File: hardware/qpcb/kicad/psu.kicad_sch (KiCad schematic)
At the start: 110 parts, among them IC1 ADM7150ARDZ-5.0-R7, IC2 ADM7150ARDZ-5.0-R7, IC3 ADM7150ARDZ-5.0-R7, IC4 ADM7150ARDZ-5.0-R7, IC5 TPS5450QDDARQ1, IC6 LT3083EQ#PBF, IC7 TPS5450QDDARQ1, IC8 LT3083EQ#PBF, J10 Conn_01x02, J3 Conn_01x02, J4 Conn_01x02, J5 Conn_01x02, J6 Conn_01x02, J7 Conn_01x02, J8 Conn_01x02, J9 Conn_01x02, Q1 2N7002, Q2 2N7002, Q3 2N7002, Q4 2N7002, Q5 2N7002, Q6 2N7002, U2 MC34063AD, U3 LM337T

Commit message: Complete PSU simulations and fix ERC errors
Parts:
- added C47, C48: C, symbol Device:C
- added C50: 0.1u, Capacitor_SMD:C_0805_2012Metric_Pad1.18x1.45mm_HandSolder, symbol Device:C_Polarized_US
- added C57, C58: 10u, Capacitor_SMD:C_0805_2012Metric_Pad1.18x1.45mm_HandSolder, symbol Device:C_Polarized_US
- added D10, D11, D12, D13, D14, D15, D16, D17: LED, symbol Device:LED
- added D18, D19, D20, D21, D24, D25: PMEG3050EP,115, symbol Device:D_Schottky
- added IC10: LT3083EQ#PBF, LT3083EQPBF, symbol LT3083EQ#PBF:LT3083EQ#PBF
- added J13, J14, J15, J16, J17: Conn_01x02, symbol Connector_Generic:Conn_01x02
- added L4, L5: L, symbol Device:L
- added R44, R45, R46, R47, R68, R69, R70, R71: R, symbol Device:R
- added R72, R73: TBD, symbol Device:R
- added TP1, TP10, TP11, TP12, TP2, TP3, TP4, TP5, TP6, TP7, TP8, TP9: TestPoint, symbol Connector:TestPoint
- R30: value 100k -> 120k
- R31: value 100k -> 6k
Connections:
- net -3V3: now also C37.2, R12.2, U3.3 (OUT), D17.1 (K)
- net 12V: now also R45.1
- net 12V_EN: now also TP1.1; no longer R31.2
- net 24V: now also J13.1 (Pin_1), R44.1
- net 3V3_A: now also R69.1
- net 3V3_A_EN: now also TP5.1
- net 3V3_B: now also R70.1
- net 3V3_B_EN: now also TP6.1
- net 3V3_RASP: no longer R30.1, R31.1
- net 5V_A: now also R47.1
- net 5V_A_EN: now also TP3.1
- net 5V_B: now also R68.1
- net 5V_B_EN: now also TP4.1
- net 6V: now also R46.1
- net 6V_EN: now also TP2.1; no longer R30.2
- net GND: now also R30.1, R31.1, C47.1, C48.1, C50.2, C57.2, C58.2, D10.1 (K), D11.1 (K), D12.1 (K), D13.1 (K), D14.1 (K), D15.1 (K), D16.1 (K), IC10.1 (NC), J13.2 (Pin_2), J14.2 (Pin_2), J15.2 (Pin_2), J16.2 (Pin_2), J17.2 (Pin_2), R71.1, R72.1, R73.1
- net 6V_AUX: now reaches C15.1, IC3.8 (VIN), R16.1
- net 6V_AUX: now also C20.1, IC4.8 (VIN), R17.1, R31.2, C58.1, IC10.3 (OUT_1), IC10.6 (OUT_2), J17.1 (Pin_1)
- net -6V_INT: now reaches C25.2, C26.2, D2.2 (A), R5.1, U2.4 (GND)
- net -6V_INT: now also D20.2 (A), TP11.1
- net 8V: now reaches C1.1, IC1.8 (VIN), R14.1
- net 8V: now also C10.1, C21.1, C24.1, IC2.8 (VIN), IC6.4 (VCONTROL), IC6.5 (IN), R15.1, R4.2, U2.6 (Vin), C57.1, D18.1 (K), D19.1 (K), IC10.4 (VCONTROL), IC10.5 (IN), TP8.1
- net -6V: now reaches C36.2, U3.2 (IN)
- net -6V: now also D20.1 (K), D21.1 (K), TP12.1
- net 13V5: no longer names the net of C30.1, L3.1, R8.2
- net 13V5: now also L5.1; no longer C34.1, IC8.4 (VCONTROL), IC8.5 (IN)
- net 7V5: no longer names the net of C29.1, L1.1, R3.2
- net 7V5: now also L4.1; no longer C21.1, IC6.4 (VCONTROL), IC6.5 (IN)
- new net: D13.2 (A), R47.2
- new net: C50.1, IC10.2 (SET), R30.2
- new net: D12.2 (A), R46.2
- new net: D14.2 (A), R68.2
- new net: D11.2 (A), R45.2
- new net: D10.2 (A), R44.2
- new net: D16.2 (A), R70.2
- new net: D15.2 (A), R69.2
- new net: D17.2 (A), R71.2
- new net -6V_EXT: D21.2 (A), J16.1 (Pin_1)
- new net 14V: C34.1, D24.1 (K), D25.1 (K), IC8.4 (VCONTROL), IC8.5 (IN), TP10.1
- new net 14V_EXT: D25.2 (A), J14.1 (Pin_1)
- new net 14V_INT: C48.2, D24.2 (A), L5.2, R73.2, TP9.1
- new net 8V_EXT: D19.2 (A), J15.1 (Pin_1)
- new net 8V_INT: C47.2, D18.2 (A), L4.2, R72.2, TP7.1
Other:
- note added: "Power input connectors"
- note added: "Power output connectors"
- note added: "Power-good LEDs"
- note added: "Test-points"
- note added: "The TPS5450-Q1 circuit was designed using TI WEBENCH POWER DESIGNER. The design can be obtained at the following link: https://webench.ti.com/appinfo/webench/scripts/SDP.cgi?ID=2D7513C0D29458C6"
- note added: "The TPS5450-Q1 circuit was designed using TI WEBENCH POWER DESIGNER. The design can be obtained at the following link: https://webench.ti.com/appinfo/webench/scripts/SDP.cgi?ID=5E5784C9527CE6F4"
- note added: "The input 24V is first converted to 14V using the TPS5450-Q1 switching voltage regulator. Then, it is further converted to 12V using the LT3083 linear voltage regulator. 14V input voltage is required to guarantee the minimum voltage dropout of the schottky diode and of the LT3083."
- note added: "The input 24V is first converted to 8V using the TPS5450-Q1 switching voltage regulator. Then, it is further converted to 6V using the LT3083 linear voltage regulator. 8V input voltage is required to guarantee the minimum voltage dropout of the schottky diode and of the LT3083."
- note removed: "The TPS5450-Q1 circuit was designed using TI WEBENCH POWER DESIGNER. The design can be obtained at the following link: https://webench.ti.com/appinfo/webench/scripts/SDP.cgi?ID=1DBFA0CBE6476B5C"
- note removed: "The TPS5450-Q1 circuit was designed using TI WEBENCH POWER DESIGNER. The design can be obtained at the following link: https://webench.ti.com/appinfo/webench/scripts/SDP.cgi?ID=32DE457FE0809D28"
- note removed: "The input 24V is first converted to 13.5V using the TPS5450-Q1 switching voltage regulator. Then, it is further converted to 12V using the LT3083 linear voltage regulator. 13.5V input voltage is required to guarantee the minimum voltage dropout."
- note removed: "The input 24V is first converted to 7.5V using the TPS5450-Q1 switching voltage regulator. Then, it is further converted to 6V using the LT3083 linear voltage regulator. 7.5V input voltage is required to guarantee the minimum voltage dropout."
- moved on the sheet: C1, C10, C11, C12, C13, C14, C15, C16, C17, C18, C19, C2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

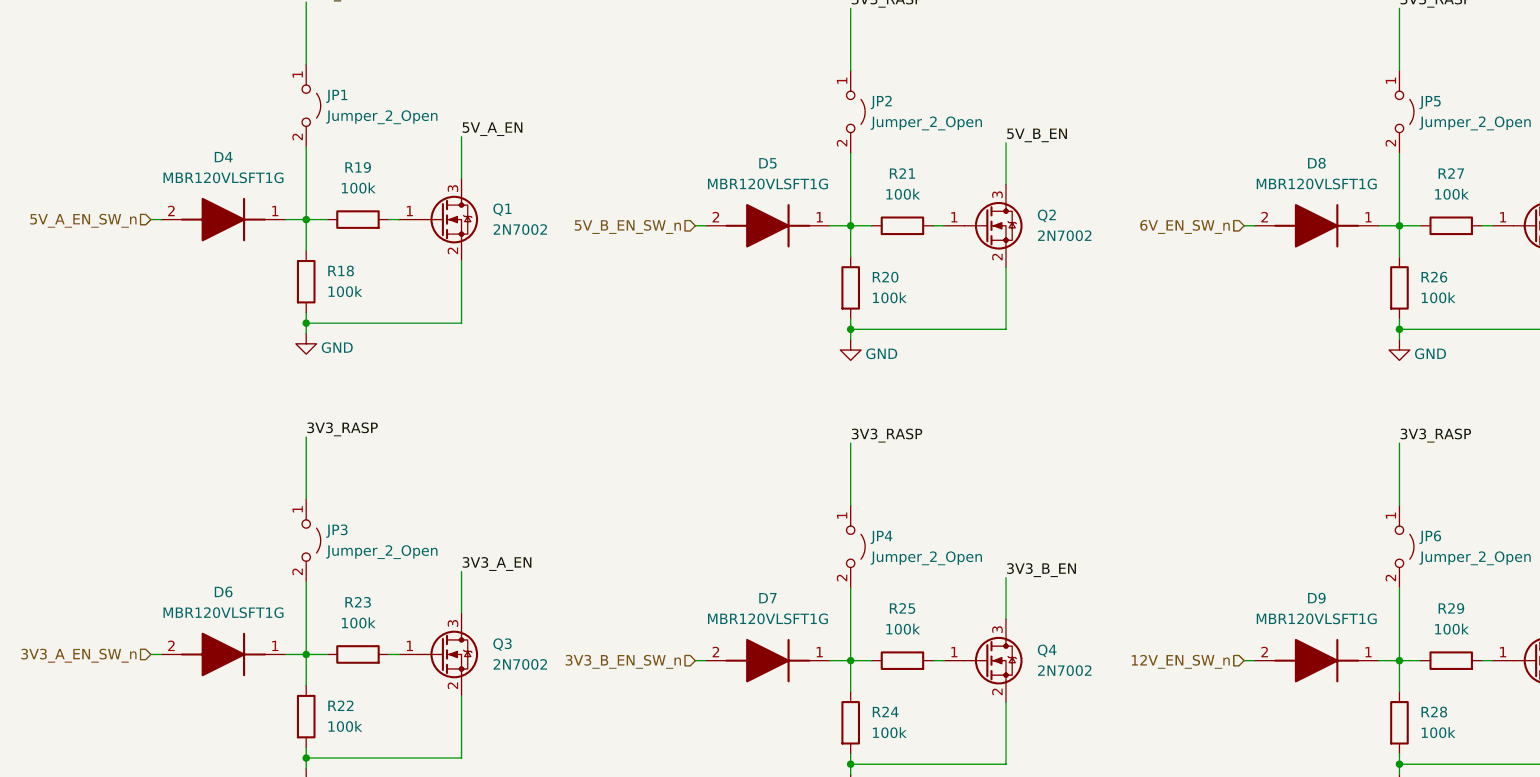
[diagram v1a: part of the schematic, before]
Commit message: Add mixer footprint and symbols
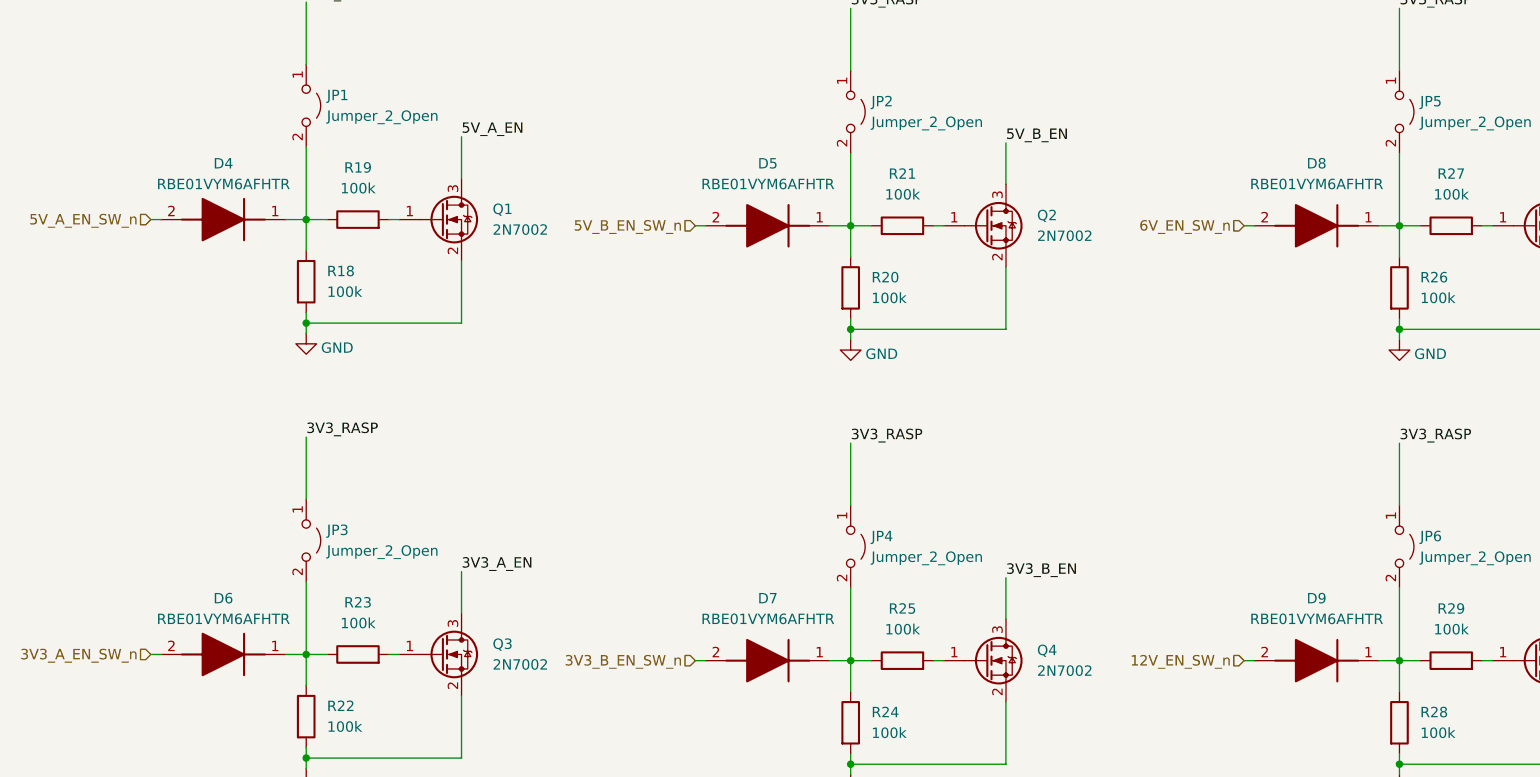
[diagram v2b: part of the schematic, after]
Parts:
- D4, D5, D6, D7, D8, D9: value MBR120VLSFT1G -> RBE01VYM6AFHTR
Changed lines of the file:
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@@
 			)
 		)
-		(property "Value" "MBR120VLSFT1G"
+		(property "Value" "RBE01VYM6AFHTR"
 			(at 115.57 355.6 0)
 			(effects
@@
 			)
 		)
-		(property "Value" "MBR120VLSFT1G"
+		(property "Value" "RBE01VYM6AFHTR"
 			(at 182.88 302.26 0)
 			(effects
@@
 		(fields_autoplaced yes)
 		(property "Reference" "D4"
-			(at 48.7882 298.9614 0)
+			(at 48.7882 299.72 0)
 			(effects
 				(font
@@
 			)
 		)
-		(property "Value" "MBR120VLSFT1G"
-			(at 48.7882 301.5014 0)
+		(property "Value" "RBE01VYM6AFHTR"
+			(at 48.7882 302.26 0)
 			(effects
 				(font
@@
 			)
 		)
-		(property "Value" "MBR120VLSFT1G"
+		(property "Value" "RBE01VYM6AFHTR"
 			(at 115.57 302.26 0)
 			(effects
@@
 			)
 		)
-		(property "Value" "MBR120VLSFT1G"
+		(property "Value" "RBE01VYM6AFHTR"
 			(at 182.88 355.6 0)
 			(effects
@@
 		(fields_autoplaced yes)
 		(property "Reference" "D6"
-			(at 48.7882 352.3014 0)
+			(at 48.7882 353.06 0)
 			(effects
 				(font
@@
 			)
 		)
-		(property "Value" "MBR120VLSFT1G"
-			(at 48.7882 354.8414 0)
+		(property "Value" "RBE01VYM6AFHTR"
+			(at 48.7882 355.6 0)
 			(effects
 				(font

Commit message: Final version of MC43063A and fill components' production info
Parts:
- added C17: 22u, Capacitor_SMD:C_0805_2012Metric_Pad1.18x1.45mm_HandSolder, symbol Device:C_Polarized_US
- added TP13, TP14, TP15, TP16, TP17, TP18, TP19, TP20: TestPoint, symbol Connector:TestPoint
- C1: renamed from C27; Manufacturer (none) -> TDK; Manufacturer Part Number (none) -> CKG57NX5R1H226M500JH; Mouser Part Number (none) -> 810-CKG57NX5R1H226M; Mouser Price/Stock (none) -> https://www.mouser.it/ProductDetail/TDK/CKG57NX5R1H226M500J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
- C10: renamed from C58; Manufacturer (none) -> TDK; Manufacturer Part Number (none) -> C3225X8R1E106K250AC; Mouser Part Number (none) -> 810-C3225X816K25AC; Mouser Price/Stock (none) -> https://www.mouser.it/ProductDetail/TDK/C3225X8R1E106K250AC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; Package (none) -> 1210
- C12: renamed from C32; Manufacturer (none) -> TDK; Manufacturer Part Number (none) -> CKG57NX5R1H226M500JH; Mouser Part Number (none) -> 810-CKG57NX5R1H226M; Mouser Price/Stock (none) -> https://www.mouser.it/ProductDetail/TDK/CKG57NX5R1H226M500J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
- C13: renamed from C34; Manufacturer (none) -> TDK; Manufacturer Part Number (none) -> C3225X8R1E106K250AC; Mouser Part Number (none) -> 810-C3225X816K25AC; Mouser Price/Stock (none) -> https://www.mouser.it/ProductDetail/TDK/C3225X8R1E106K250AC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; Package (none) -> 1210
- C14: renamed from C31; Manufacturer (none) -> KYOCERA AVX; Manufacturer Part Number (none) -> 08055C103KAT2A; Mouser Part Number (none) -> 581-08055C103K; Mouser Price/Stock (none) -> https://www.mouser.it/ProductDetail/KYOCERA-AVX/08055C103KA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; Package (none) -> 0805
- C15: renamed from C35; Manufacturer (none) -> TDK; Manufacturer Part Number (none) -> C3225X8R1E106K250AC; Mouser Part Number (none) -> 810-C3225X816K25AC; Mouser Price/Stock (none) -> https://www.mouser.it/ProductDetail/TDK/C3225X8R1E106K250AC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; Package (none) -> 1210
- C16: renamed from C30; value 68u -> 22u; Manufacturer (none) -> KYOCERA AVX; Manufacturer Part Number (none) -> TPSB226K020R0400; Mouser Part Number (none) -> 581-TPSB226K020R0400; Mouser Price/Stock (none) -> https://www.mouser.it/ProductDetail/KYOCERA-AVX/TPSB226K020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; Package (none) -> 1210
- C22: renamed from C48; value C -> 10u; Manufacturer (none) -> KEMET; Manufacturer Part Number (none) -> T491C106M020AT; Mouser Part Number (none) -> 80-T491C106M020; Mouser Price/Stock (none) -> https://www.mouser.it/ProductDetail/KEMET/T491C106M020AT?qs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; Package (none) -> 2412
- C3: renamed from C21; Manufacturer (none) -> TDK; Manufacturer Part Number (none) -> C3225X8R1E106K250AC; Mouser Part Number (none) -> 810-C3225X816K25AC; Mouser Price/Stock (none) -> https://www.mouser.it/ProductDetail/TDK/C3225X8R1E106K250AC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; Package (none) -> 1210
- C31: renamed from C26; value 100u -> 190p; Manufacturer (none) -> KYOCERA AVX; Manufacturer Part Number (none) -> 700A191JCA150XC100; Mouser Part Number (none) -> 581-700A191JCA150100; Mouser Price/Stock (none) -> https://www.mouser.it/ProductDetail/KYOCERA-AVX/700A191JCA1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; Package (none) -> 0505
- C38: renamed from C37; Manufacturer (none) -> KYOCERA AVX; Manufacturer Part Number (none) -> TAJP106K010RNJ; Mouser Part Number (none) -> 581-TAJP106K010RNJ; Mouser Price/Stock (none) -> https://www.mouser.it/ProductDetail/KYOCERA-AVX/TAJP106K010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; Package (none) -> 0805
- C39: renamed from C25; value 100u -> 750u; Manufacturer (none) -> Nichicon; Manufacturer Part Number (none) -> UCZ1J751MNS1MS; Mouser Part Number (none) -> 647-UCZ1J751MNS1MS; Mouser Price/Stock (none) -> https://www.mouser.it/ProductDetail/Nichicon/UCZ1J751MNS1MS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
- C4: renamed from C28; Manufacturer (none) -> KYOCERA AVX; Manufacturer Part Number (none) -> 08055C103KAT2A; Mouser Part Number (none) -> 581-08055C103K; Mouser Price/Stock (none) -> https://www.mouser.it/ProductDetail/KYOCERA-AVX/08055C103KA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; Package (none) -> 0805
- C5: renamed from C23; Manufacturer (none) -> TDK; Manufacturer Part Number (none) -> C3225X8R1E106K250AC; Mouser Part Number (none) -> 810-C3225X816K25AC; Mouser Price/Stock (none) -> https://www.mouser.it/ProductDetail/TDK/C3225X8R1E106K250AC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; Package (none) -> 1210
- C6: renamed from C29; value 220u -> 150u
- C7: renamed from C47; value C -> 10u; Manufacturer (none) -> KEMET; Manufacturer Part Number (none) -> T491C106M020AT; Mouser Part Number (none) -> 80-T491C106M020; Mouser Price/Stock (none) -> https://www.mouser.it/ProductDetail/KEMET/T491C106M020AT?qs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; Package (none) -> 2412
- C9: renamed from C57; Manufacturer (none) -> TDK; Manufacturer Part Number (none) -> C3225X8R1E106K250AC; Mouser Part Number (none) -> 810-C3225X816K25AC; Mouser Price/Stock (none) -> https://www.mouser.it/ProductDetail/TDK/C3225X8R1E106K250AC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; Package (none) -> 1210
- D1: renamed from D10; Manufacturer (none) -> Bivar; Manufacturer Part Number (none) -> SM0805GC; Mouser Part Number (none) -> 749-SM0805GC; Mouser Price/Stock (none) -> https://www.mouser.it/ProductDetail/Bivar/SM0805GC?qs=sGAEp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; Package (none) -> 0805
- D10: renamed from D7; footprint SODFL3616X98N -> footprints:SODFL3616X98N; Manufacturer (none) -> ROHM Semiconductor; Manufacturer Part Number (none) -> RBE01VYM6AFHTR; Manufacturer_Name onsemi -> (none); Manufacturer_Part_Number MBR120VLSFT1G -> (none); Mouser Part Number 863-MBR120VLSFT1G -> 755-RBE01VYM6AFHTR; Mouser Price/Stock https://www.mouser.co.uk/ProductDetail/onsemi/MBR120VLSFT1G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 -> https://www.mouser.it/ProductDetail/ROHM-Semiconductor/RBE0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; Package (none) -> SOD-323-HE-2
- D11: renamed from D15; Manufacturer (none) -> Bivar; Manufacturer Part Number (none) -> SM0805GC; Mouser Part Number (none) -> 749-SM0805GC; Mouser Price/Stock (none) -> https://www.mouser.it/ProductDetail/Bivar/SM0805GC?qs=sGAEp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; Package (none) -> 0805
- D12: renamed from D16; Manufacturer (none) -> Bivar; Manufacturer Part Number (none) -> SM0805GC; Mouser Part Number (none) -> 749-SM0805GC; Mouser Price/Stock (none) -> https://www.mouser.it/ProductDetail/Bivar/SM0805GC?qs=sGAEp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; Package (none) -> 0805
- D13: renamed from D17; Manufacturer (none) -> Bivar; Manufacturer Part Number (none) -> SM0805GC; Mouser Part Number (none) -> 749-SM0805GC; Mouser Price/Stock (none) -> https://www.mouser.it/ProductDetail/Bivar/SM0805GC?qs=sGAEp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; Package (none) -> 0805
- D14: renamed from D18; Manufacturer (none) -> Nexperia; Manufacturer Part Number (none) -> PMEG3050EP,115; Mouser Part Number (none) -> 771-PMEG3050EP115; Mouser Price/Stock (none) -> https://www.mouser.it/ProductDetail/Nexperia/PMEG3050EP115?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; Package (none) -> SOD-128-2
- D15: renamed from D19; Manufacturer (none) -> Nexperia; Manufacturer Part Number (none) -> PMEG3050EP,115; Mouser Part Number (none) -> 771-PMEG3050EP115; Mouser Price/Stock (none) -> https://www.mouser.it/ProductDetail/Nexperia/PMEG3050EP115?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; Package (none) -> SOD-128-2
- D16: renamed from D8; footprint SODFL3616X98N -> footprints:SODFL3616X98N; Manufacturer (none) -> ROHM Semiconductor; Manufacturer Part Number (none) -> RBE01VYM6AFHTR; Manufacturer_Name onsemi -> (none); Manufacturer_Part_Number MBR120VLSFT1G -> (none); Mouser Part Number 863-MBR120VLSFT1G -> 755-RBE01VYM6AFHTR; Mouser Price/Stock https://www.mouser.co.uk/ProductDetail/onsemi/MBR120VLSFT1G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 -> https://www.mouser.it/ProductDetail/ROHM-Semiconductor/RBE0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; Package (none) -> SOD-323-HE-2
- D17: renamed from D9; footprint SODFL3616X98N -> footprints:SODFL3616X98N; Manufacturer (none) -> ROHM Semiconductor; Manufacturer Part Number (none) -> RBE01VYM6AFHTR; Manufacturer_Name onsemi -> (none); Manufacturer_Part_Number MBR120VLSFT1G -> (none); Mouser Part Number 863-MBR120VLSFT1G -> 755-RBE01VYM6AFHTR; Mouser Price/Stock https://www.mouser.co.uk/ProductDetail/onsemi/MBR120VLSFT1G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 -> https://www.mouser.it/ProductDetail/ROHM-Semiconductor/RBE0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; Package (none) -> SOD-323-HE-2
- D18: renamed from D3; value B540C-13-F -> SS24FL; Manufacturer (none) -> Onsemi/Fairchild; Manufacturer Part Number (none) -> SS24FL; Mouser Part Number (none) -> 512-SS24FL; Mouser Price/Stock (none) -> https://www.mouser.it/ProductDetail/onsemi-Fairchild/SS24FL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; Package (none) -> SOD-123-2
- D19: renamed from D24; footprint (none) -> Diode_SMD:D_SOD-128; Manufacturer (none) -> Nexperia; Manufacturer Part Number (none) -> PMEG3050EP,115; Mouser Part Number (none) -> 771-PMEG3050EP115; Mouser Price/Stock (none) -> https://www.mouser.it/ProductDetail/Nexperia/PMEG3050EP115?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; Package (none) -> SOD-128-2
- D2: renamed from D11; Manufacturer (none) -> Bivar; Manufacturer Part Number (none) -> SM0805GC; Mouser Part Number (none) -> 749-SM0805GC; Mouser Price/Stock (none) -> https://www.mouser.it/ProductDetail/Bivar/SM0805GC?qs=sGAEp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; Package (none) -> 0805
- D20: renamed from D25; Manufacturer (none) -> Nexperia; Manufacturer Part Number (none) -> PMEG3050EP,115; Mouser Part Number (none) -> 771-PMEG3050EP115; Mouser Price/Stock (none) -> https://www.mouser.it/ProductDetail/Nexperia/PMEG3050EP115?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; Package (none) -> SOD-128-2
- D21: renamed from D2; Manufacturer (none) -> Diodes Incorporated; Manufacturer Part Number (none) -> 1N5819HWQ-7-F; Mouser Part Number (none) -> 621-1N5819HWQ-7-F; Mouser Price/Stock (none) -> https://www.mouser.it/ProductDetail/Diodes-Incorporated/1N5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; Package (none) -> SOD-123-2
- D22: renamed from D20; Manufacturer (none) -> Nexperia; Manufacturer Part Number (none) -> PMEG3050EP,115; Mouser Part Number (none) -> 771-PMEG3050EP115; Mouser Price/Stock (none) -> https://www.mouser.it/ProductDetail/Nexperia/PMEG3050EP115?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; Package (none) -> SOD-128-2
- D23: renamed from D21; Manufacturer (none) -> Nexperia; Manufacturer Part Number (none) -> PMEG3050EP,115; Mouser Part Number (none) -> 771-PMEG3050EP115; Mouser Price/Stock (none) -> https://www.mouser.it/ProductDetail/Nexperia/PMEG3050EP115?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; Package (none) -> SOD-128-2
- D3: renamed from D4; footprint SODFL3616X98N -> footprints:SODFL3616X98N; Manufacturer (none) -> ROHM Semiconductor; Manufacturer Part Number (none) -> RBE01VYM6AFHTR; Manufacturer_Name onsemi -> (none); Manufacturer_Part_Number MBR120VLSFT1G -> (none); Mouser Part Number 863-MBR120VLSFT1G -> 755-RBE01VYM6AFHTR; Mouser Price/Stock https://www.mouser.co.uk/ProductDetail/onsemi/MBR120VLSFT1G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 -> https://www.mouser.it/ProductDetail/ROHM-Semiconductor/RBE0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; Package (none) -> SOD-323-HE-2
- D4: renamed from D6; footprint SODFL3616X98N -> footprints:SODFL3616X98N; Manufacturer (none) -> ROHM Semiconductor; Manufacturer Part Number (none) -> RBE01VYM6AFHTR; Manufacturer_Name onsemi -> (none); Manufacturer_Part_Number MBR120VLSFT1G -> (none); Mouser Part Number 863-MBR120VLSFT1G -> 755-RBE01VYM6AFHTR; Mouser Price/Stock https://www.mouser.co.uk/ProductDetail/onsemi/MBR120VLSFT1G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 -> https://www.mouser.it/ProductDetail/ROHM-Semiconductor/RBE0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; Package (none) -> SOD-323-HE-2
- D5: renamed from D12; Manufacturer (none) -> Bivar; Manufacturer Part Number (none) -> SM0805GC; Mouser Part Number (none) -> 749-SM0805GC; Mouser Price/Stock (none) -> https://www.mouser.it/ProductDetail/Bivar/SM0805GC?qs=sGAEp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; Package (none) -> 0805
- D6: renamed from D1; Manufacturer (none) -> Diodes Incorporated; Manufacturer Part Number (none) -> SBR10200CTL-13; Mouser Part Number (none) -> 621-SBR10200CTL-13; Mouser Price/Stock (none) -> https://www.mouser.it/ProductDetail/Diodes-Incorporated/SBR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; Package (none) -> DPAK-3 (TO-252-3)
- D7: renamed from D13; Manufacturer (none) -> Bivar; Manufacturer Part Number (none) -> SM0805GC; Mouser Part Number (none) -> 749-SM0805GC; Mouser Price/Stock (none) -> https://www.mouser.it/ProductDetail/Bivar/SM0805GC?qs=sGAEp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; Package (none) -> 0805
- D8: renamed from D14; Manufacturer (none) -> Bivar; Manufacturer Part Number (none) -> SM0805GC; Mouser Part Number (none) -> 749-SM0805GC; Mouser Price/Stock (none) -> https://www.mouser.it/ProductDetail/Bivar/SM0805GC?qs=sGAEp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; Package (none) -> 0805
- D9: renamed from D5; footprint SODFL3616X98N -> footprints:SODFL3616X98N; Manufacturer (none) -> ROHM Semiconductor; Manufacturer Part Number (none) -> RBE01VYM6AFHTR; Manufacturer_Name onsemi -> (none); Manufacturer_Part_Number MBR120VLSFT1G -> (none); Mouser Part Number 863-MBR120VLSFT1G -> 755-RBE01VYM6AFHTR; Mouser Price/Stock https://www.mouser.co.uk/ProductDetail/onsemi/MBR120VLSFT1G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 -> https://www.mouser.it/ProductDetail/ROHM-Semiconductor/RBE0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; Package (none) -> SOD-323-HE-2
- IC1: renamed from IC6; footprint LT3083EQPBF -> footprints:LT3083EQPBF; Manufacturer (none) -> Analog Devices; Manufacturer_Name Analog Devices -> (none); Manufacturer_Part_Number LT3083EQ#PBF -> (none); Package (none) -> DDPAK-5
- IC2: renamed from IC5; footprint SOIC127P600X170-9N -> footprints:SOIC127P600X170-9N; Manufacturer (none) -> Texas Instruments; Manufacturer Part Number (none) -> TPS5450QDDARQ1; Manufacturer_Name Texas Instruments -> (none); Manufacturer_Part_Number TPS5450QDDARQ1 -> (none); Package (none) -> SO-PowerPad-8
- IC3: renamed from IC10; footprint LT3083EQPBF -> footprints:LT3083EQPBF; Manufacturer (none) -> Analog Devices; Manufacturer_Name Analog Devices -> (none); Manufacturer_Part_Number LT3083EQ#PBF -> (none); Package (none) -> DDPAK-5
- IC4: renamed from IC8; footprint LT3083EQPBF -> footprints:LT3083EQPBF; Manufacturer (none) -> Analog Devices; Manufacturer_Name Analog Devices -> (none); Manufacturer_Part_Number LT3083EQ#PBF -> (none); Package (none) -> DDPAK-5
- IC5: renamed from IC7; footprint SOIC127P600X170-9N -> footprints:SOIC127P600X170-9N; Manufacturer (none) -> Texas Instruments; Manufacturer Part Number (none) -> TPS5450QDDARQ1; Manufacturer_Name Texas Instruments -> (none); Manufacturer_Part_Number TPS5450QDDARQ1 -> (none); Package (none) -> SO-PowerPad-8
- IC6: renamed from IC3; value ADM7150ARDZ-5.0-R7 -> ADM7150ARDZ-3.3-R7; footprint SOIC127P600X175-9N -> footprints:SOIC127P600X175-9N; Manufacturer (none) -> Analog Devices; Manufacturer Part Number (none) -> ADM7150ARDZ-3.3-R7; Manufacturer_Name Analog Devices -> (none); Manufacturer_Part_Number ADM7150ARDZ-5.0-R7 -> (none); Mouser Part Number 584-ADM7150ARDZ5.0R7 -> 584-ADM7150ARDZ3.3R7; Package (none) -> SOIC-8
- IC7: renamed from IC4; value ADM7150ARDZ-5.0-R7 -> ADM7150ARDZ-3.3-R7; footprint SOIC127P600X175-9N -> footprints:SOIC127P600X175-9N; Manufacturer (none) -> Analog Devices; Manufacturer Part Number (none) -> ADM7150ARDZ-3.3-R7; Manufacturer_Name Analog Devices -> (none); Manufacturer_Part_Number ADM7150ARDZ-5.0-R7 -> (none); Mouser Part Number 584-ADM7150ARDZ5.0R7 -> 584-ADM7150ARDZ3.3R7; Package (none) -> SOIC-8
- IC8: renamed from IC1; footprint SOIC127P600X175-9N -> footprints:SOIC127P600X175-9N; Manufacturer (none) -> Analog Devices; Manufacturer Part Number (none) -> ADM7150ARDZ-5.0-R7; Manufacturer_Name Analog Devices -> (none); Manufacturer_Part_Number ADM7150ARDZ-5.0-R7 -> (none); Package (none) -> SOIC-8
- IC9: renamed from IC2; footprint SOIC127P600X175-9N -> footprints:SOIC127P600X175-9N; Manufacturer (none) -> Analog Devices; Manufacturer Part Number (none) -> ADM7150ARDZ-5.0-R7; Manufacturer_Name Analog Devices -> (none); Manufacturer_Part_Number ADM7150ARDZ-5.0-R7 -> (none); Package (none) -> SOIC-8
- L1: Manufacturer (none) -> Coilcraft; Manufacturer Part Number (none) -> MSS1210-153MED; Mouser Part Number (none) -> 994-MSS1210-153MED; Mouser Price/Stock (none) -> https://www.mouser.it/ProductDetail/Coilcraft/MSS1210-153ME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; Package (none) -> 4747 (1212 metric)
- L2: renamed from L4; value L -> 10u; Manufacturer (none) -> Bourns; Manufacturer Part Number (none) -> SRP1038WA-100M; Mouser Part Number (none) -> 652-SRP1038WA-100M; Mouser Price/Stock (none) -> https://www.mouser.it/ProductDetail/Bourns/SRP1038WA-100M?q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
- L3: value 22u -> 33u
- L4: renamed from L5; value L -> 10u; Manufacturer (none) -> Bourns; Manufacturer Part Number (none) -> SRP1038WA-100M; Mouser Part Number (none) -> 652-SRP1038WA-100M; Mouser Price/Stock (none) -> https://www.mouser.it/ProductDetail/Bourns/SRP1038WA-100M?q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
- L5: renamed from L2; value L -> 95u; Manufacturer (none) -> Panasonic; Manufacturer Part Number (none) -> ETQ-P5M101YGM; Mouser Part Number (none) -> 667-ETQ-P5M101YGM; Mouser Price/Stock (none) -> https://www.mouser.it/ProductDetail/Panasonic/ETQ-P5M101YGM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
- Q1, Q4, Q5, Q6: Manufacturer (none) -> onsemi/Fairchild; Manufacturer Part Number (none) -> 2N7002; Mouser Part Number (none) -> 512-2N7002; Mouser Price/Stock (none) -> https://www.mouser.it/ProductDetail/onsemi-Fairchild/2N7002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; Package (none) -> SOT-23-3
- Q2: renamed from Q3; Manufacturer (none) -> onsemi/Fairchild; Manufacturer Part Number (none) -> 2N7002; Mouser Part Number (none) -> 512-2N7002; Mouser Price/Stock (none) -> https://www.mouser.it/ProductDetail/onsemi-Fairchild/2N7002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; Package (none) -> SOT-23-3
- Q3: renamed from Q2; Manufacturer (none) -> onsemi/Fairchild; Manufacturer Part Number (none) -> 2N7002; Mouser Part Number (none) -> 512-2N7002; Mouser Price/Stock (none) -> https://www.mouser.it/ProductDetail/onsemi-Fairchild/2N7002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; Package (none) -> SOT-23-3
- R11: renamed from R7; value 1.96k -> 1.8k
- R28: renamed from R10; Manufacturer (none) -> Panasonic; Manufacturer Part Number (none) -> ERA-6AED244V; Mouser Part Number (none) -> 667-ERA-6AED244V; Mouser Price/Stock (none) -> https://www.mouser.it/ProductDetail/Panasonic/ERA-6AED244V?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
- R31: renamed from R9; value 1k -> 953; Manufacturer (none) -> Vishay; Manufacturer Part Number (none) -> CRCW0805953RFKEA; Mouser Part Number (none) -> 71-CRCW0805-953-E3; Mouser Price/Stock (none) -> https://www.mouser.it/ProductDetail/Vishay-Dale/CRCW0805953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
- R35: renamed from R4; value R -> 787m; Manufacturer (none) -> TE Connectivity; Manufacturer Part Number (none) -> RLC73K3AR787FTDF; Mouser Part Number (none) -> 279-RLC73K3AR787FTDF; Mouser Price/Stock (none) -> https://www.mouser.it/ProductDetail/TE-Connectivity-CGS/RLC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; Package (none) -> 2512
- R36: renamed from R5; value R -> 2.4k; Manufacturer (none) -> Panasonic; Manufacturer Part Number (none) -> ERA-6ARW242V; Mouser Part Number (none) -> 667-ERA-6ARW242V; Mouser Price/Stock (none) -> https://www.mouser.it/ProductDetail/Panasonic/ERA-6ARW242V?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
- R37: renamed from R6; value R -> 9.1k; Manufacturer (none) -> Panasonic; Manufacturer Part Number (none) -> ERA-6ARW912V; Mouser Part Number (none) -> 667-ERA-6ARW912V; Mouser Price/Stock (none) -> https://www.mouser.it/ProductDetail/Panasonic/ERA-6ARW912V?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
- U2: Manufacturer (none) -> Texas Instruments; Manufacturer Part Number (none) -> MC34063ADG4; Mouser Part Number (none) -> 595-MC34063ADG4; Mouser Price/Stock (none) -> https://www.mouser.it/ProductDetail/Texas-Instruments/MC340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; Package (none) -> SOIC-8
- U3: value LM337T -> LT337TAT; Manufacturer (none) -> Analog Devices; Manufacturer Part Number (none) -> LT337AT#PBF; Mouser Part Number (none) -> 584-LT337AT#PBF; Mouser Price/Stock (none) -> https://www.mouser.it/ProductDetail/Analog-Devices/LT337ATP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; Package TO-220-3 Texas Instruments -> TO-220-3
- renumbered C33 to C11, C11 to C18, C16 to C19, C22 to C2, C12 to C20, C17 to C21, C13 to C23, C18 to C24, C14 to C25, C19 to C26, C24 to C27, C36 to C28, C15 to C29, C20 to C30, C3 to C32, C6 to C33, C5 to C34, C7 to C35, C4 to C36, C8 to C37, C2 to C40, C9 to C41, C1 to C42, C10 to C43, C50 to C8, J17 to J10, J6 to J11, J7 to J12, J8 to J13, J9 to J14, J10 to J15, J13 to J3, J14 to J4, J15 to J5, J16 to J6, J3 to J7, J4 to J8, J5 to J9, JP3 to JP2, JP2 to JP3, R3 to R10, R2 to R12, R68 to R13, R69 to R14, R20 to R15, R24 to R16, R21 to R17, R25 to R18, R30 to R19, R44 to R2, R72 to R20, R70 to R21, R71 to R22, R26 to R23, R28 to R24, R31 to R25, R27 to R26, R29 to R27, R11 to R29, R45 to R3, R8 to R30, R73 to R32, R16 to R33, R17 to R34, R13 to R38, R12 to R39, R18 to R4, R14 to R40, R15 to R41, R22 to R5, R19 to R6, R23 to R7, R46 to R8, R47 to R9, TP11 to TP10, TP6 to TP11, TP7 to TP2, TP2 to TP3, TP8 to TP4, TP3 to TP5, TP9 to TP6, TP4 to TP7, TP10 to TP8, TP5 to TP9
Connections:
- net -3V3: now also TP20.1
- net 12V: now also TP13.1
- net 3V3_A: now also TP18.1
- net 3V3_B: now also TP19.1
- net 5V_A: now also TP16.1
- net 5V_B: now also TP17.1
- net 6V: now also TP14.1
- net 6V_AUX: now also TP15.1
- net GND: now also C17.2
- net at C16.1, L3.1, L4.1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: now also C17.1
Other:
- moved on the sheet: C22, L4, R32
